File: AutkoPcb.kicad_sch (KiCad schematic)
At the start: 8 parts, among them J101 Conn_01x06_Male, J102 Conn_01x04_Male, J103 Conn_01x05_Male, J104 Conn_01x04_Male, J105 Conn_01x02_Male, J106 Conn_01x02_Male, J107 Conn_01x02_Male, J108 Conn_01x05_Male

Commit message: [FEAT] schematic and alyout finished but need to be revieved
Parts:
- added J104, J105: Conn_01x04_Male, Connector_PinHeader_2.54mm:PinHeader_1x04_P2.54mm_Vertical, symbol Connector:Conn_01x04_Male
- added J106: Conn_01x11_Male, Connector_PinSocket_2.54mm:PinSocket_1x11_P2.54mm_Vertical, symbol Connector:Conn_01x11_Male
- renumbered J103 to J107, J104 to J108, J105 to J109, J106 to J110, J107 to J111, J108 to J112
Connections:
- net +3.3V: now also J104.1 (Pin_1), J105.1 (Pin_1), J106.1 (Pin_1)
- net GND: now also J104.4 (Pin_4), J105.4 (Pin_4), J106.11 (Pin_11)
- new net A0_NC: J106.5 (Pin_5)
- new net A10_NC: J106.4 (Pin_4)
- new net A11_NC: J106.3 (Pin_3)
- new net A15_NC: J106.2 (Pin_2)
- new net A1_NC: J106.6 (Pin_6)
- new net A6_NC: J106.7 (Pin_7)
- new net A7_NC: J106.8 (Pin_8)
- new net A8_NC: J106.9 (Pin_9)
- new net A9_NC: J106.10 (Pin_10)
- new net RX1_NC: J104.3 (Pin_3)
- new net RX2_NC: J105.3 (Pin_3)
- new net TX1_NC: J104.2 (Pin_2)
- new net TX2_NC: J105.2 (Pin_2)
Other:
- sheet Tensee ports: added A0_NC, A10_NC, A11_NC, A15_NC, A1_NC, A6_NC, A7_NC, A8_NC, A9_NC, D+_NC, D-_NC, ON_OFF_NC, PROGRAM_NC, RX1_NC, RX2_NC, TX1_NC, TX2_NC, VIN_NC, VUSB_NC; removed none

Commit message: update plików
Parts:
- removed J110: Conn_01x02_Male, Connector_JST:JST_XH_B2B-XH-A_1x02_P2.50mm_Vertical, symbol Connector:Conn_01x02_Male
- added J? (x2): JST 2.56mm, symbol Connector:Conn_01x03_Male
- added J? (x2): JST 2.56mm, Connector_JST:JST_XH_B2B-XH-A_1x02_P2.50mm_Vertical, symbol Connector:Conn_01x02_Male
- added R102, R104, R? (x2): 4.7k, Resistor_THT:R_Axial_DIN0204_L3.6mm_D1.6mm_P7.62mm_Horizontal, symbol Device:R
- J101: value Conn_01x06_Male -> JST 2.56mm
- J102: value Conn_01x04_Male -> JST 2.56mm
- J103: renamed from J104; value Conn_01x04_Male -> JST 2.56mm
- J104: renamed from J105; value Conn_01x04_Male -> JST 2.56mm
- J106: renamed from J107; value Conn_01x05_Male -> JST 2.56mm
- J107: renamed from J108; value Conn_01x04_Male -> JST 2.56mm
- J108: renamed from J109; value Conn_01x02_Male -> JST 2.56mm
- J110: renamed from J111; value Conn_01x02_Male -> JST 2.56mm
- J111: renamed from J112; value Conn_01x05_Male -> JST 2.56mm
- renumbered J106 to J105
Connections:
- net +3.3V: now also R102.2, R104.2, R?.2, R?.2
- net GND: now also J?.2 (Pin_2), J?.2 (Pin_2), J?.3 (Pin_3), J?.3 (Pin_3)
- net IMU_SCL: now also R102.1
- net IMU_SDA: now also R104.1
- net TOF_SCL: now also R?.1
- net TOF_SDA: now also R?.1
- new net: J?.1 (Pin_1), J?.1 (Pin_1)
- new net SPEED1: J?.1 (Pin_1)
- new net SPEED2: J?.1 (Pin_1)
- new net STEERING1: J?.2 (Pin_2)
- new net STEERING2: J?.2 (Pin_2)
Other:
- sheet Tensee ports: added SPEED1, SPEED2, STEERING1, STEERING2; removed SPEED, STEERING, VIN_NC
- company: (none) -> Szymon Przybył
- title: (none) -> Main schematic
- moved on the sheet: J103, J104, J105, J106, J108, J110, J111

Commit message: schematic update after meeting
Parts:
- removed J105: Conn_01x11_Male, Connector_PinSocket_2.54mm:PinSocket_1x11_P2.54mm_Vertical, symbol Connector:Conn_01x11_Male
- removed J108, J110: JST 2.56mm, Connector_JST:JST_XH_B2B-XH-A_1x02_P2.50mm_Vertical, symbol Connector:Conn_01x02_Male
- added J105: JST 2.56mm, Connector_JST:JST_XH_B4B-XH-A_1x04_P2.50mm_Vertical, symbol Connector:Conn_01x04_Male
- added J106: Conn_01x10_Male, Connector_PinHeader_2.54mm:PinHeader_1x10_P2.54mm_Vertical, symbol Connector:Conn_01x10_Male
- J112, J113: renamed from J?; footprint (none) -> Connector_JST:JST_XH_B3B-XH-A_1x03_P2.50mm_Vertical
- gave numbers to parts that had none: 4
- renumbered J106 to J109, J107 to J110, R102 to R101, R104 to R103
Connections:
- net +3.3V: now also J106.1 (Pin_1)
- net A0_NC: now also J106.6 (Pin_6)
- net A10_NC: now also J106.5 (Pin_5)
- net A11_NC: now also J106.4 (Pin_4)
- net A15_NC: now also J106.3 (Pin_3)
- net A1_NC: now also J106.7 (Pin_7)
- net A6_NC: now also J106.8 (Pin_8)
- net A7_NC: now also J106.9 (Pin_9)
- net D+_NC: now also J105.3 (Pin_3)
- net D-_NC: now also J105.2 (Pin_2)
- net GND: now also J105.4 (Pin_4), J106.10 (Pin_10)
- net V_USB_NC: now also J105.1 (Pin_1)
- new net A16_NC: J106.2 (Pin_2)
- no-connect marks 0 -> 2
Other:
- sheet Tensee ports: added A16_NC; removed A8_NC, A9_NC, VOLTMETER
- moved on the sheet: J107, J108, J111, J112, J113

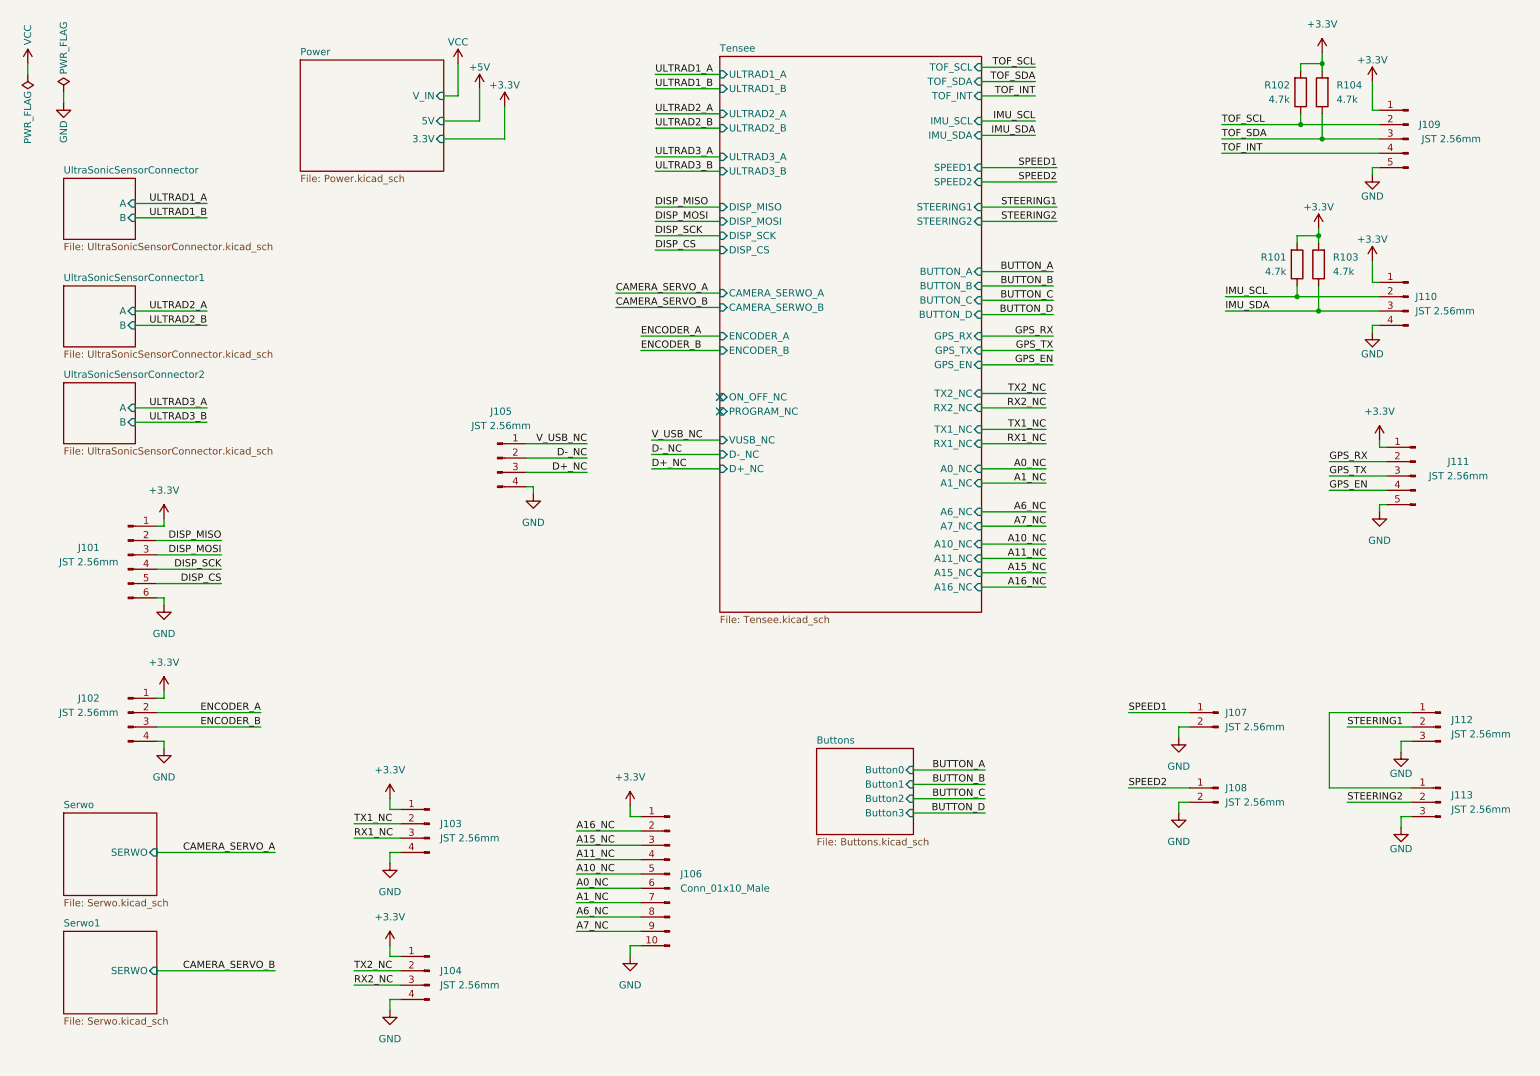
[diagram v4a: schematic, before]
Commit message: layout update moved power section to the bottom of the board, ibom generated, changed footprint for switches
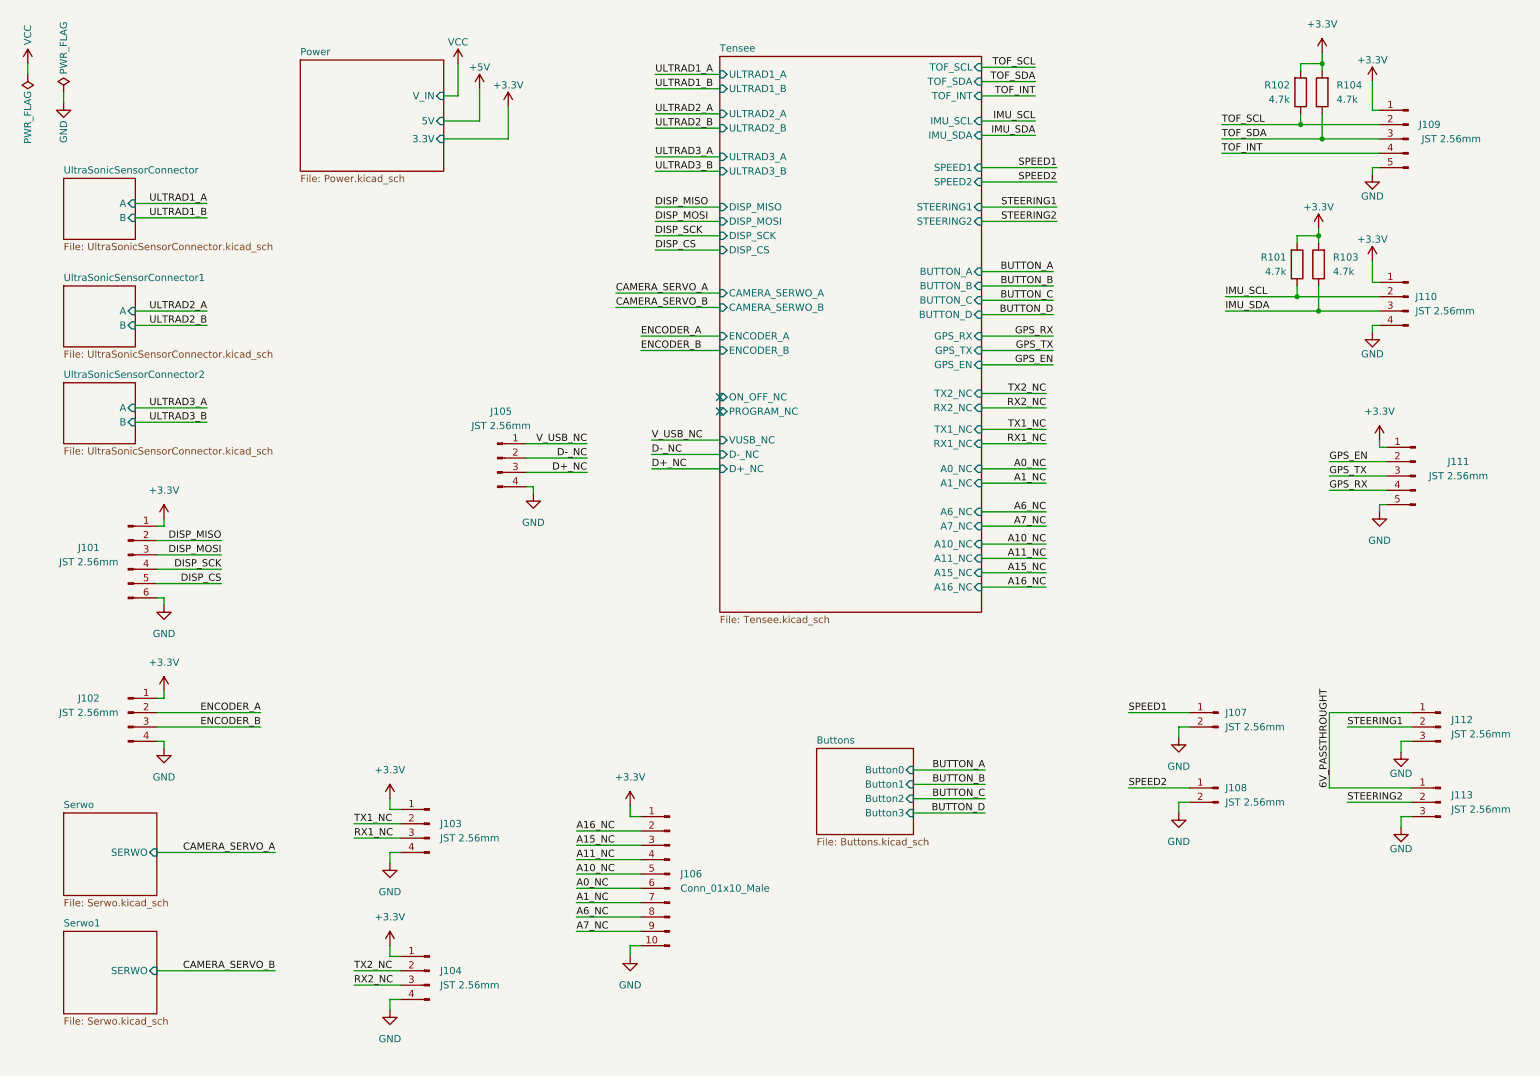
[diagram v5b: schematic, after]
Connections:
- net GPS_EN: now also J111.2 (Pin_2); no longer J111.4 (Pin_4)
- net GPS_RX: now also J111.4 (Pin_4); no longer J111.2 (Pin_2)
- net 6V_PASSTHROUGHT: now reaches J112.1 (Pin_1), J113.1 (Pin_1)

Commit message: final board candidate
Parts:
- removed J106: Conn_01x10_Male, Connector_PinHeader_2.54mm:PinHeader_1x10_P2.54mm_Vertical, symbol Connector:Conn_01x10_Male
- added J114: Conn_01x12_Pin, Connector_PinSocket_2.54mm:PinSocket_1x12_P2.54mm_Vertical, symbol Connector:Conn_01x12_Pin
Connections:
- net +3.3V: now also J114.1 (Pin_1), J114.2 (Pin_2)
- net A0_NC: now also J114.7 (Pin_7)
- net A10_NC: now also J114.6 (Pin_6)
- net A11_NC: now also J114.5 (Pin_5)
- net A15_NC: now also J114.4 (Pin_4)
- net A16_NC: now also J114.3 (Pin_3)
- net A1_NC: now also J114.8 (Pin_8)
- net A6_NC: now also J114.9 (Pin_9)
- net A7_NC: now also J114.10 (Pin_10)
- net GND: now also J114.11 (Pin_11), J114.12 (Pin_12)

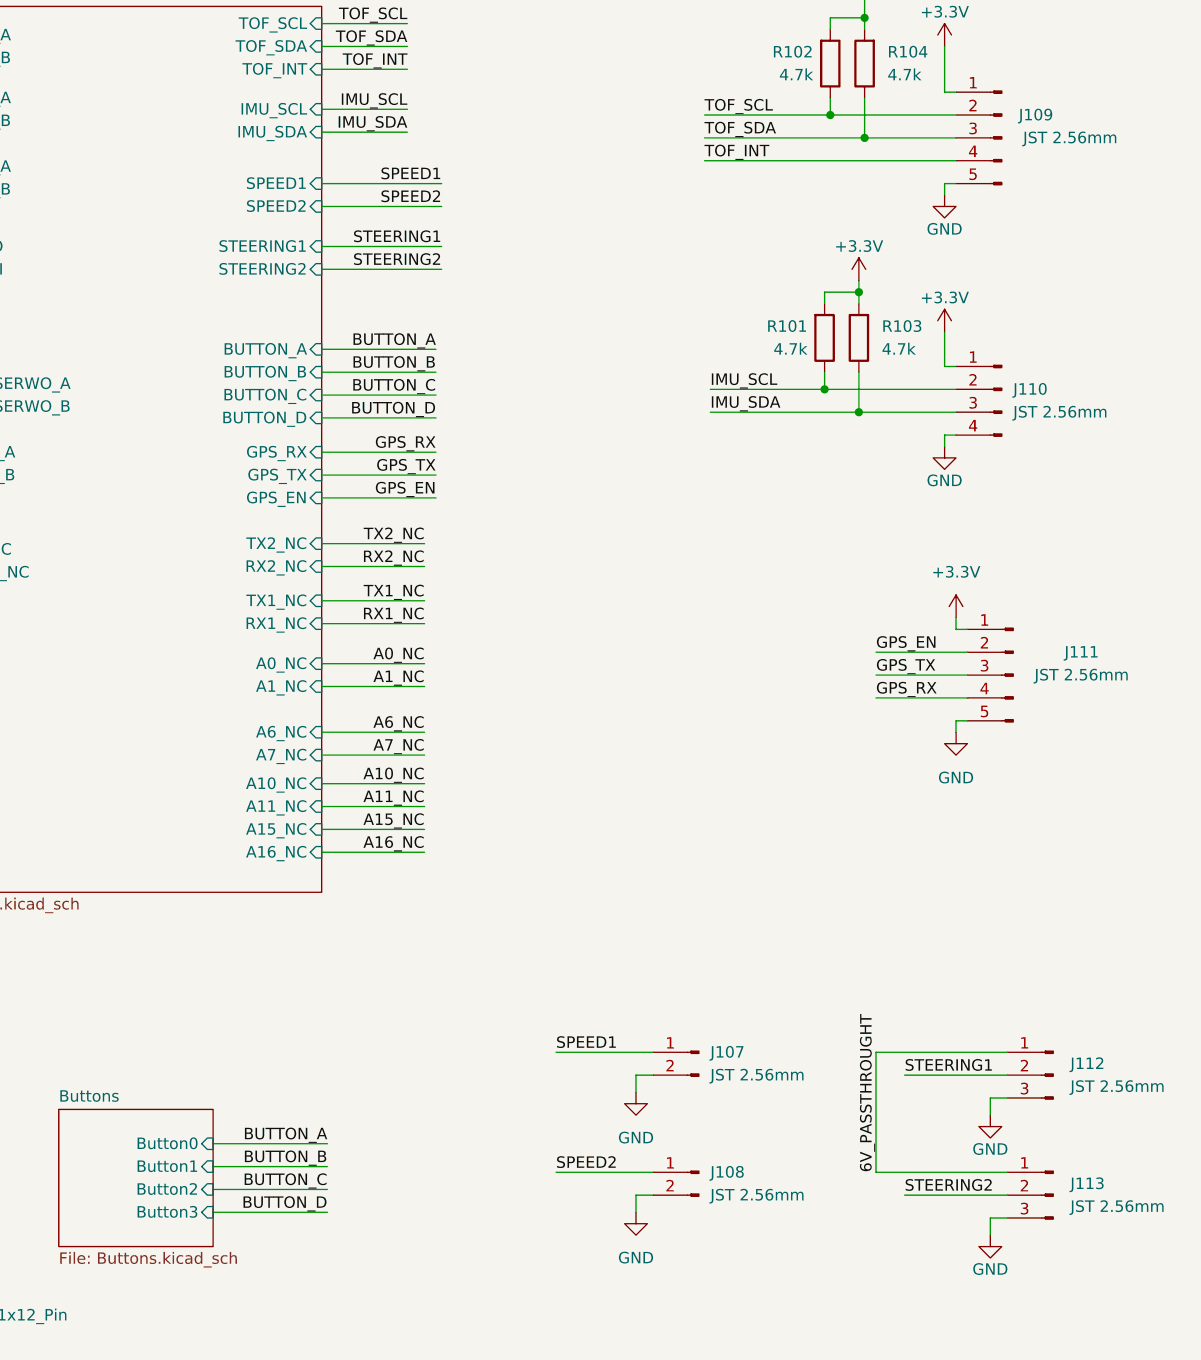
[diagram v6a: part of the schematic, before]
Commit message: changing labels on PCB
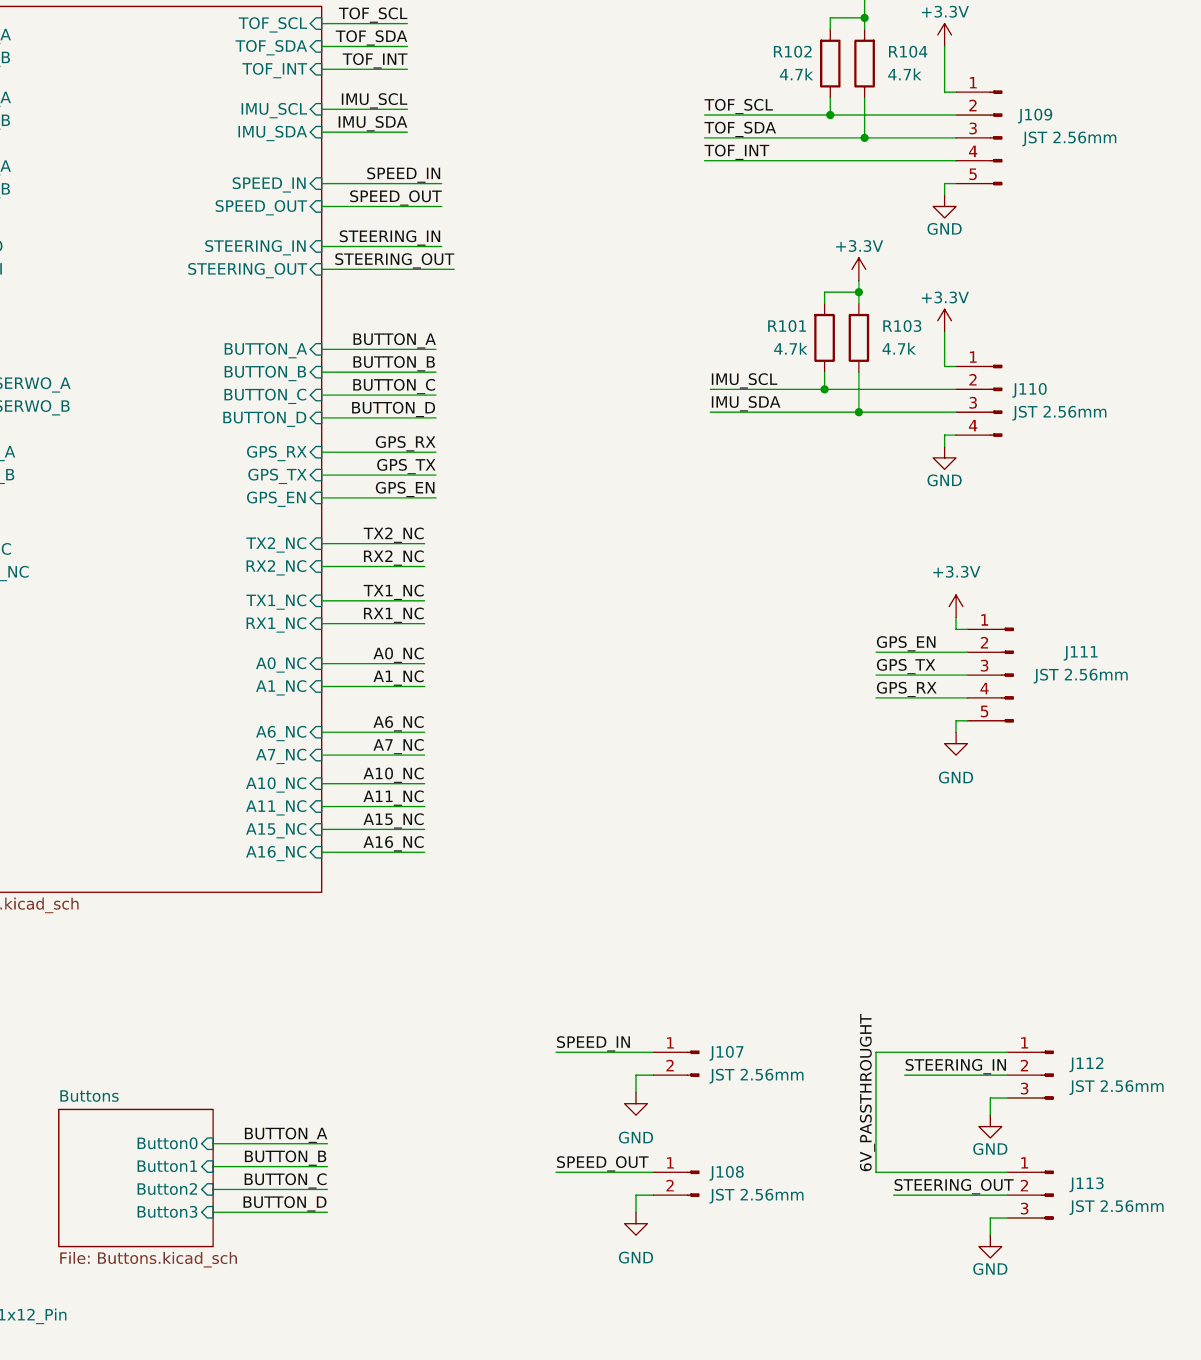
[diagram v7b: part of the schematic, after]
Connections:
- net SPEED1 renamed SPEED_IN
- net SPEED2 renamed SPEED_OUT
- net STEERING1 renamed STEERING_IN
- net STEERING2 renamed STEERING_OUT
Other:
- sheet Tensee ports: added SPEED_IN, SPEED_OUT, STEERING_IN, STEERING_OUT; removed SPEED1, SPEED2, STEERING1, STEERING2
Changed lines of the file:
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@@
     (stroke (width 0) (type default))
   )
-  (wire (pts (xy 249.555 151.765) (xy 260.985 151.765))
+  (wire (pts (xy 248.3278 151.765) (xy 260.985 151.765))
     (stroke (width 0) (type default))
   )
@@
     (stroke (width 0) (type default))
   )
-  (wire (pts (xy 184.785 48.895) (xy 198.12 48.895))
+  (wire (pts (xy 184.785 48.895) (xy 199.5137 48.895))
     (stroke (width 0) (type default))
   )
@@
     (effects (font (size 1.27 1.27)) (justify right bottom))
   )
-  (label "SPEED1" (at 198.12 39.37 180) (fields_autoplaced)
+  (label "SPEED_IN" (at 198.12 39.37 180) (fields_autoplaced)
     (effects (font (size 1.27 1.27)) (justify right bottom))
   )
@@
     (effects (font (size 1.27 1.27)) (justify right bottom))
   )
-  (label "STEERING1" (at 249.555 138.43 0) (fields_autoplaced)
+  (label "STEERING_IN" (at 249.555 138.43 0) (fields_autoplaced)
     (effects (font (size 1.27 1.27)) (justify left bottom))
   )
@@
     (effects (font (size 1.27 1.27)) (justify left bottom))
   )
-  (label "SPEED2" (at 198.12 41.91 180) (fields_autoplaced)
+  (label "SPEED_OUT" (at 198.12 41.91 180) (fields_autoplaced)
     (effects (font (size 1.27 1.27)) (justify right bottom))
   )
@@
     (effects (font (size 1.27 1.27)) (justify right bottom))
   )
-  (label "STEERING2" (at 249.555 151.765 0) (fields_autoplaced)
+  (label "STEERING_OUT" (at 248.3278 151.765 0) (fields_autoplaced)
     (effects (font (size 1.27 1.27)) (justify left bottom))
   )
@@
     (effects (font (size 1.27 1.27)) (justify right bottom))
   )
-  (label "SPEED1" (at 210.82 135.89 0) (fields_autoplaced)
+  (label "SPEED_IN" (at 210.82 135.89 0) (fields_autoplaced)
     (effects (font (size 1.27 1.27)) (justify left bottom))
   )
@@
     (effects (font (size 1.27 1.27)) (justify right bottom))
   )
-  (label "STEERING2" (at 198.12 48.895 180) (fields_autoplaced)
+  (label "STEERING_OUT" (at 199.5137 48.895 180) (fields_autoplaced)
     (effects (font (size 1.27 1.27)) (justify right bottom))
   )
@@
     (effects (font (size 1.27 1.27)) (justify left bottom))
   )
-  (label "SPEED2" (at 210.82 149.225 0) (fields_autoplaced)
+  (label "SPEED_OUT" (at 210.82 149.225 0) (fields_autoplaced)
     (effects (font (size 1.27 1.27)) (justify left bottom))
   )
@@
     (effects (font (size 1.27 1.27)) (justify left bottom))
   )
-  (label "STEERING1" (at 198.12 46.355 180) (fields_autoplaced)
+  (label "STEERING_IN" (at 198.12 46.355 180) (fields_autoplaced)
     (effects (font (size 1.27 1.27)) (justify right bottom))
   )
@@
       (effects (font (size 1.27 1.27)) (justify right))
     )
-    (pin "SPEED1" input (at 184.785 39.37 0)
-      (effects (font (size 1.27 1.27)) (justify right))
-    )
-    (pin "STEERING1" input (at 184.785 46.355 0)
-      (effects (font (size 1.27 1.27)) (justify right))
-    )
-    (pin "SPEED2" input (at 184.785 41.91 0)
-      (effects (font (size 1.27 1.27)) (justify right))
-    )
-    (pin "STEERING2" input (at 184.785 48.895 0)
-      (effects (font (size 1.27 1.27)) (justify right))
-    )
+    (pin "SPEED_IN" input (at 184.785 39.37 0)
+      (effects (font (size 1.27 1.27)) (justify right))
+    )
+    (pin "STEERING_IN" input (at 184.785 46.355 0)
+      (effects (font (size 1.27 1.27)) (justify right))
+    )
+    (pin "SPEED_OUT" input (at 184.785 41.91 0)
+      (effects (font (size 1.27 1.27)) (justify right))
+    )
+    (pin "STEERING_OUT" input (at 184.785 48.895 0)
+      (effects (font (size 1.27 1.27)) (justify right))
+    )
